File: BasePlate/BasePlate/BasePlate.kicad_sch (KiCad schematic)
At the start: 10 parts, among them J1 JST_BM04B-GHS-TBT, J2 1586842-6, J3 JST_BM03B-GHS-TBT, J4 JST_BM04B-GHS-TBT, J5 JST_BM04B-GHS-TBT, J6 JST_BM04B-GHS-TBT, J7 JST_BM04B-GHS-TBT, J8 JST_BM04B-GHS-TBT

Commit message: mostly finished
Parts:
- removed J8: JST_BM04B-GHS-TBT, bots:JST_BM04B-GHS-TBT, symbol thebots_symlib:JST_BM04B-GHS-TBT
- added H1, H2, H3, H4, H5, H6, H7, H8: MountingHole_Pad, TestPoint:TestPoint_Pad_D4.0mm, symbol Mechanical:MountingHole_Pad
- added J8: Conn_01x03_Socket, Connector_PinSocket_2.54mm:PinSocket_1x03_P2.54mm_Vertical, symbol Connector:Conn_01x03_Socket
- added J9: Conn_01x02_Socket, Connector_PinSocket_2.54mm:PinSocket_1x02_P2.54mm_Vertical, symbol Connector:Conn_01x02_Socket
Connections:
- net CAN+ is gone; now on net CAN_P: J1.2, JP1.1 (A)
- net CAN- is gone; now on net CAN_N: J1.3, R1.2
- net +5V: now also J8.2 (Pin_2), J9.1 (Pin_1)
- net BKBM: now also J8.1 (Pin_1)
- net GND: now also H1.1, H3.1, H5.1, H7.1, J8.3 (Pin_3), J9.2 (Pin_2)
- net VCC: now also H2.1, H4.1, H6.1, H8.1
- net CAN_P: now reaches J6.2
- net CAN_P: now also J4.2, J5.2, J7.2
- net CAN_N: now reaches J6.3
- net CAN_N: now also J4.3, J5.3, J7.3
- no-connect marks 14 -> 11

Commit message: baseplate
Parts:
- removed H1, H2, H3, H4, H5, H6, H7, H8: MountingHole_Pad, TestPoint:TestPoint_Pad_D4.0mm, symbol Mechanical:MountingHole_Pad
- removed JP1: Jumper_2_Bridged, Connector_PinHeader_2.54mm:PinHeader_1x02_P2.54mm_Vertical, symbol thebots_symlib:Jumper_2_Bridged
- added H1, H2, H3, H4, H5, H6, H7, H8: SMD_Pad_VBAT, thebots_baseplate:TestPoint_Pad_D4.0mm, symbol thebots_symlib:SMD_Pad_VBAT
- added JP1: Jumper_2_Bridged_smd, thebots_baseplate:PinHeader_1x02_P2.54mm_Vertical_SMD_Pin1Left, symbol thebots_symlib:Jumper_2_Bridged_smd
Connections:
- net CAN_P: now also JP1.1 (A)
- net GND: now also H1.1, H3.1, H5.1, H7.1
- net VCC: now also H2.1, H4.1, H6.1, H8.1
- net at R1.1: now also JP1.2 (B)

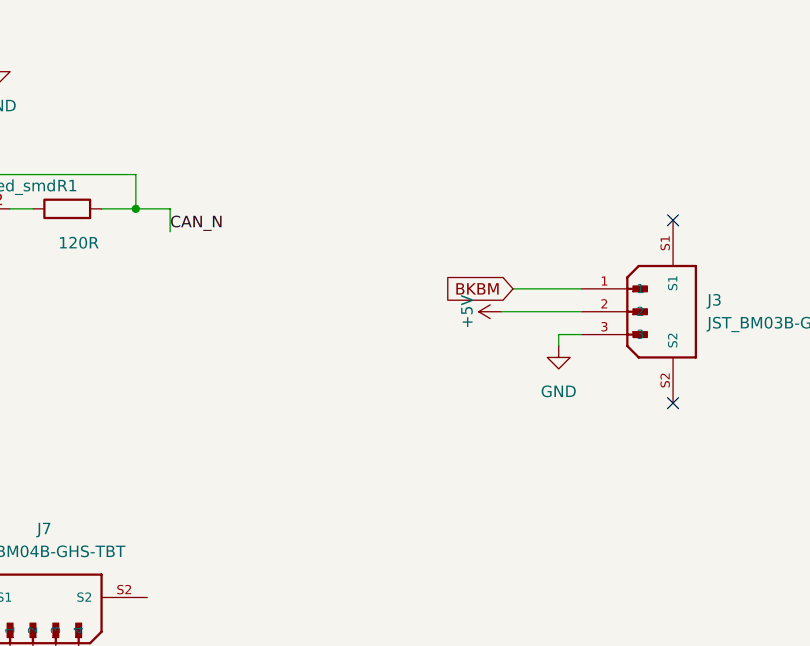
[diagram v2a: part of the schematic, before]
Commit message: wip breakbeam voltage divider
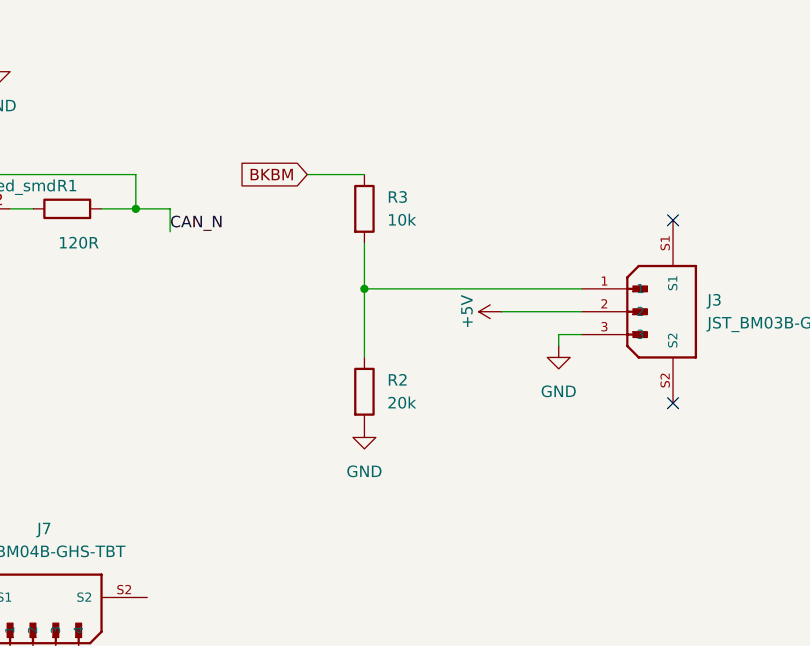
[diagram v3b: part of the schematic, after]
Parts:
- added R2: 20k, Resistor_SMD:R_0603_1608Metric, symbol Device:R
- added R3: 10k, Resistor_SMD:R_0603_1608Metric, symbol Device:R
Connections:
- net BKBM: now also R3.1; no longer J3.1
- net GND: now also R2.2
- new net: J3.1, R2.1, R3.2
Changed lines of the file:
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@@
+	)
+	(junction
+		(at 162.56 124.46)
+		(diameter 0)
+		(color 0 0 0 0)
 	)
 	(junction
@@
 	(wire
 		(pts
+			(xy 156.21 111.76) (xy 162.56 111.76)
+		)
+		(stroke
+			(width 0)
+			(type default)
+		)
+	)
+	(wire
+		(pts
 			(xy 123.19 115.57) (xy 125.73 115.57)
 		)
@@
 	(wire
 		(pts
+			(xy 162.56 119.38) (xy 162.56 124.46)
+		)
+		(stroke
+			(width 0)
+			(type default)
+		)
+	)
+	(wire
+		(pts
 			(xy 184.15 86.36) (xy 184.15 91.44)
 		)
@@
 	(wire
 		(pts
+			(xy 162.56 124.46) (xy 186.69 124.46)
+		)
+		(stroke
+			(width 0)
+			(type default)
+		)
+	)
+	(wire
+		(pts
 			(xy 171.45 78.74) (xy 171.45 83.82)
 		)
@@
 	(wire
 		(pts
-			(xy 179.07 124.46) (xy 186.69 124.46)
-		)
-		(stroke
-			(width 0)
-			(type default)
-		)
-	)
-	(wire
-		(pts
 			(xy 109.22 90.17) (xy 111.76 90.17)
 		)
@@
 		(pts
 			(xy 140.97 115.57) (xy 137.16 115.57)
+		)
+		(stroke
+			(width 0)
+			(type default)
+		)
+	)
+	(wire
+		(pts
+			(xy 162.56 124.46) (xy 162.56 132.08)
 		)
 		(stroke
@@
 	(global_label "BKBM"
 		(shape input)
-		(at 179.07 124.46 180)
+		(at 156.21 111.76 180)
 		(fields_autoplaced yes)
 		(effects
@@
 		)
 		(property "Intersheetrefs" "${INTERSHEET_REFS}"
-			(at 170.8234 124.46 0)
+			(at 147.9634 111.76 0)
 			(effects
 				(font
@@
 				(path "/bbc21205-8f0b-4bb2-8208-e4469bfb9468"
 					(reference "J2")
+					(unit 1)
+				)
+			)
+		)
+	)
+	(symbol
+		(lib_id "power:GND")
+		(at 162.56 139.7 0)
+		(unit 1)
+		(exclude_from_sim no)
+		(in_bom yes)
+		(on_board yes)
+		(dnp no)
+		(fields_autoplaced yes)
+		(property "Reference" "#PWR019"
+			(at 162.56 146.05 0)
+			(effects
+				(font
+					(size 1.27 1.27)
+				)
+				(hide yes)
+			)
+		)
+		(property "Value" "GND"
+			(at 162.56 144.78 0)
+			(effects
+				(font
+					(size 1.27 1.27)
+				)
+			)
+		)
+		(property "Footprint" ""
+			(at 162.56 139.7 0)
+			(effects
+				(font
+					(size 1.27 1.27)
+				)
+				(hide yes)
+			)
+		)
+		(property "Datasheet" ""
+			(at 162.56 139.7 0)
+			(effects
+				(font
+					(size 1.27 1.27)
+				)
+				(hide yes)
+			)
+		)
+		(property "Description" ""
+			(at 162.56 139.7 0)
+			(effects
+				(font
+					(size 1.27 1.27)
+				)
+				(hide yes)
+			)
+		)
+		(pin "1"
+		)
+		(instances
+			(project "BasePlate"
+				(path "/bbc21205-8f0b-4bb2-8208-e4469bfb9468"
+					(reference "#PWR019")
+					(unit 1)
+				)
+			)
+		)
+	)
+	(symbol
+		(lib_id "Device:R")
+		(at 162.56 115.57 0)
+		(unit 1)
+		(exclude_from_sim no)
+		(in_bom yes)
+		(on_board yes)
+		(dnp no)
+		(fields_autoplaced yes)
+		(property "Reference" "R3"
+			(at 165.1 114.2999 0)
+			(effects
+				(font
+					(size 1.27 1.27)
+				)
+				(justify left)
+			)
+		)
+		(property "Value" "10k"
+			(at 165.1 116.8399 0)
+			(effects
+				(font
+					(size 1.27 1.27)
+				)
+				(justify left)
+			)
+		)
+		(property "Footprint" "Resistor_SMD:R_0603_1608Metric"
+			(at 160.782 115.57 90)
+			(effects
+				(font
+					(size 1.27 1.27)
+				)
+				(hide yes)
+			)
+		)
+		(property "Datasheet" "~"
+			(at 162.56 115.57 0)
+			(effects
+				(font
+					(size 1.27 1.27)
+				)
+				(hide yes)
+			)
+		)
+		(property "Description" "Resistor"
+			(at 162.56 115.57 0)
+			(effects
+				(font
+					(size 1.27 1.27)
+				)
+				(hide yes)
+			)
+		)
+		(pin "1"
+		)
+		(pin "2"
+		)
+		(instances
+			(project "BasePlate"
+				(path "/bbc21205-8f0b-4bb2-8208-e4469bfb9468"
+					(reference "R3")
 					(unit 1)
 				)
@@
 					(unit 1)
 				)
+			)
+		)
+	)
+	(symbol
+		(lib_id "Device:R")
+		(at 162.56 135.89 0)
+		(unit 1)
+		(exclude_from_sim no)
+		(in_bom yes)
+		(on_board yes)
+		(dnp no)
+		(fields_autoplaced yes)
+		(property "Reference" "R2"
+			(at 165.1 134.6199 0)
+			(effects
+				(font
+					(size 1.27 1.27)
+				)
+				(justify left)
+			)
+		)
+		(property "Value" "20k"
+			(at 165.1 137.1599 0)
+			(effects
+				(font
+					(size 1.27 1.27)
+				)
+				(justify left)
+			)
+		)
+		(property "Footprint" "Resistor_SMD:R_0603_1608Metric"
+			(at 160.782 135.89 90)
+			(effects
+				(font
+					(size 1.27 1.27)
+				)
+				(hide yes)
+			)
+		)
+		(property "Datasheet" "~"
+			(at 162.56 135.89 0)
+			(effects
+				(font
+					(size 1.27 1.27)
+				)
+				(hide yes)
+			)
+		)
+		(property "Description" "Resistor"
+			(at 162.56 135.89 0)
+			(effects
+				(font
+					(size 1.27 1.27)
+				)
+				(hide yes)
+			)
+		)
+		(pin "1"
+		)
+		(pin "2"
+		)
+		(instances
+			(project "BasePlate"
+				(path "/bbc21205-8f0b-4bb2-8208-e4469bfb9468"
+					(reference "R2")
+					(unit 1)
+				)

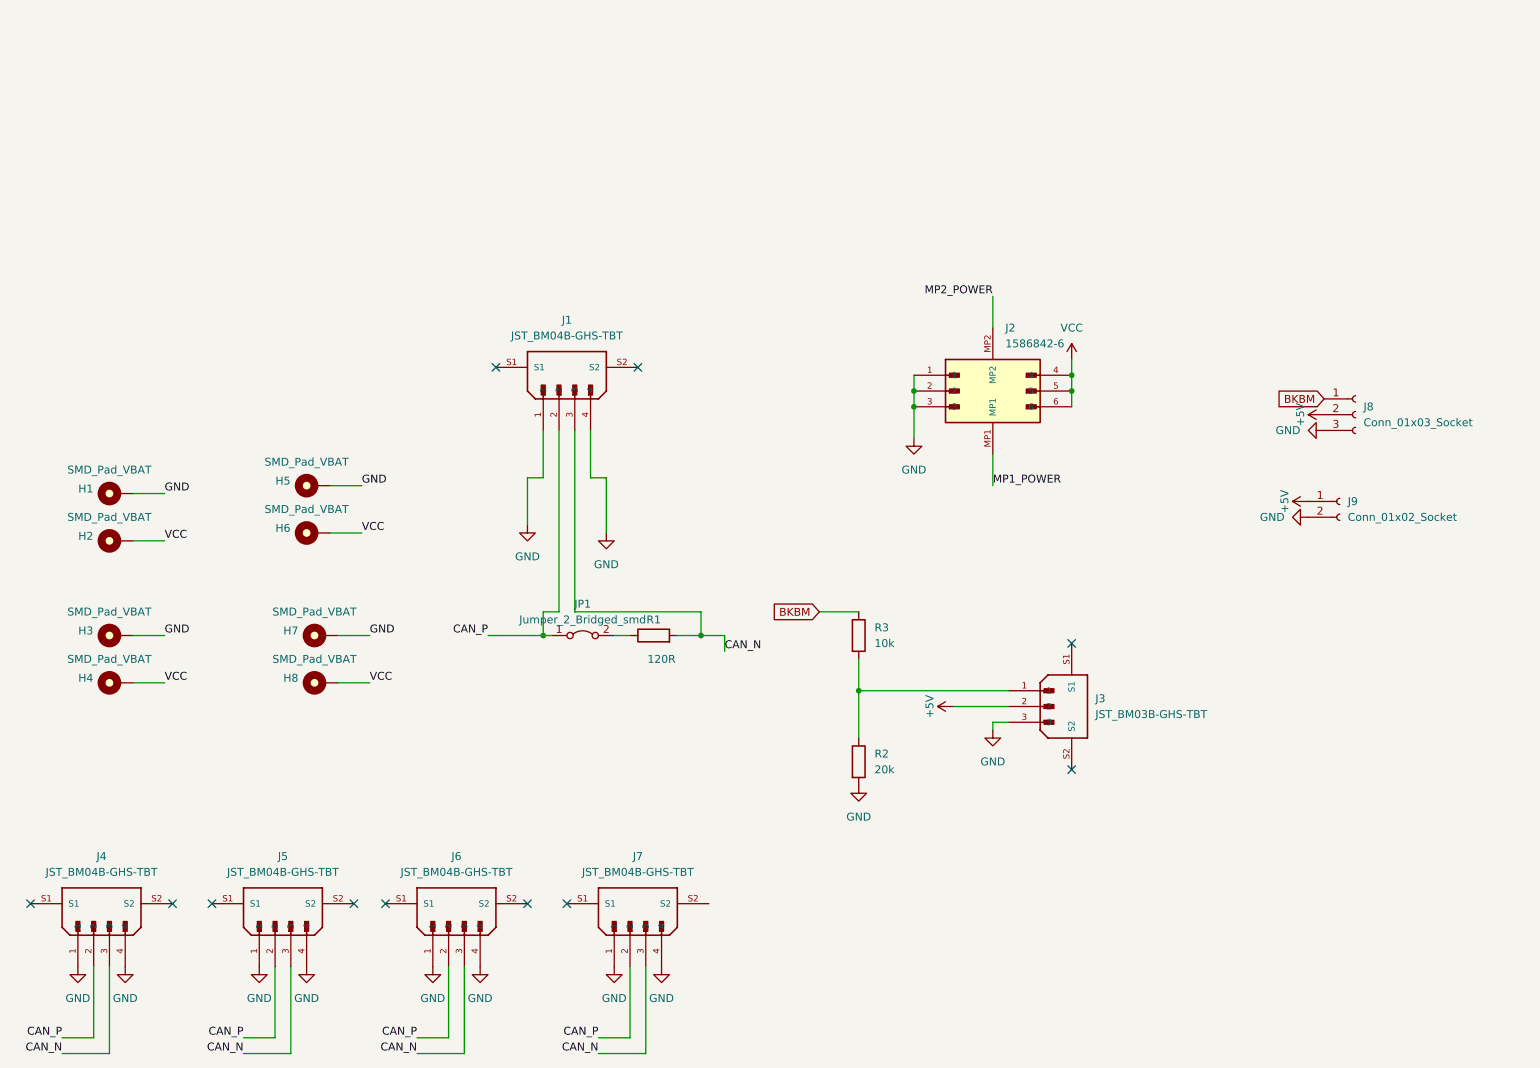
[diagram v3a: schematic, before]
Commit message: skidplate, then realized its pointless
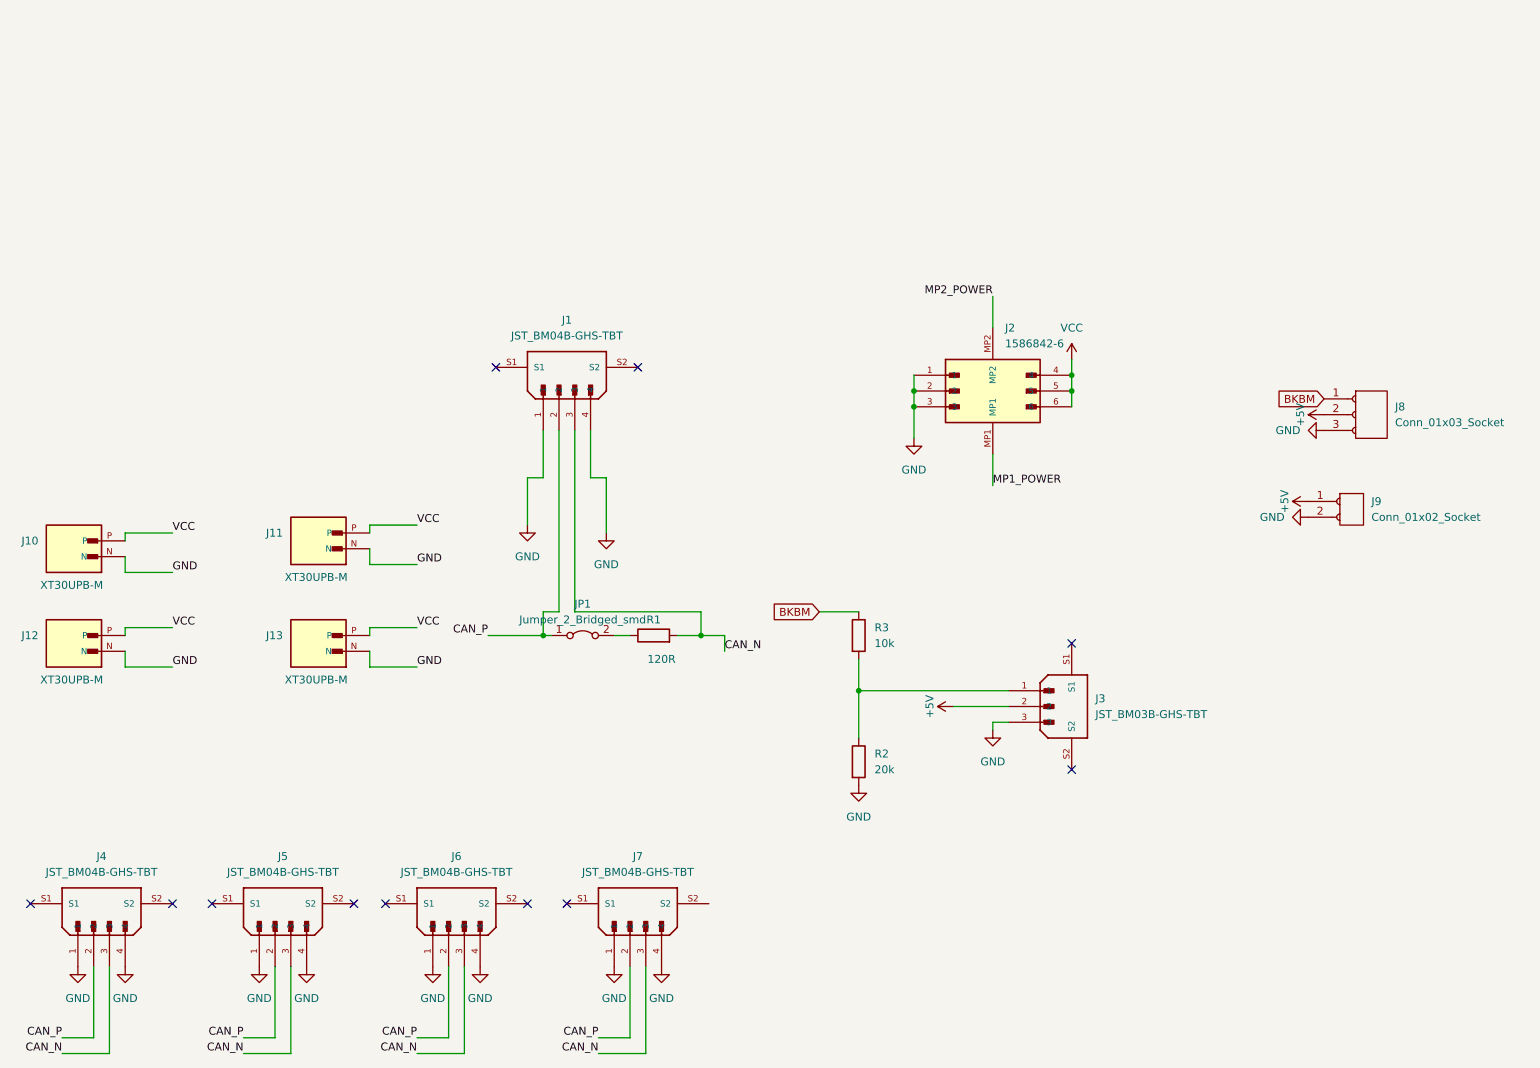
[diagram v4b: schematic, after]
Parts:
- removed H1, H2, H3, H4, H5, H6, H7, H8: SMD_Pad_VBAT, thebots_baseplate:TestPoint_Pad_D4.0mm, symbol thebots_symlib:SMD_Pad_VBAT
- added J10, J11, J12, J13: XT30UPB-M, bots:AMASS_XT30UPB-M, symbol bots:XT30UPB-M
- J1, J4, J5, J6, J7: symbol thebots_symlib:JST_BM04B-GHS-TBT -> bots:JST_BM04B-GHS-TBT
- J2: symbol thebots_symlib:TE_1586842-6_6PIN -> bots:TE_1586842-6_6PIN
- J3: symbol thebots_symlib:JST_BM03B-GHS-TBT -> bots:JST_BM03B-GHS-TBT
- J8: footprint Connector_PinSocket_2.54mm:PinSocket_1x03_P2.54mm_Vertical -> bots:PinSocket_1x03_P2.54mm_Vertical; symbol Connector:Conn_01x03_Socket -> bots:Conn_01x03_Socket
- J9: footprint Connector_PinSocket_2.54mm:PinSocket_1x02_P2.54mm_Vertical -> bots:PinSocket_1x02_P2.54mm_Vertical; symbol Connector:Conn_01x02_Socket -> bots:Conn_01x02_Socket
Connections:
- net GND: now also J10.N, J11.N, J12.N, J13.N
- net VCC: now also J10.P, J11.P, J12.P, J13.P

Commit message: baseplate
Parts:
- removed JP1: Jumper_2_Bridged_smd, thebots_baseplate:PinHeader_1x02_P2.54mm_Vertical_SMD_Pin1Left, symbol thebots_symlib:Jumper_2_Bridged_smd
- added JP1: Jumper_2_Bridged_smd, bots:PinHeader_1x02_P2.54mm_Vertical_SMD_Pin1Left, symbol bots:Jumper_2_Bridged_smd
- added R4: 0R, bots:R_0603_1608Metric, symbol bots:R_0R
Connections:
- net CAN_P: now also R4.1
- net jumper_N: now reaches R1.1
- net jumper_N: now also JP1.1 (A)
- new net jumper_P: JP1.2 (B), R4.2
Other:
- note added: "Matching resistor for length"
- moved on the sheet: J1, R1

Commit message: baseplate v1.1
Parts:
- removed J8: Conn_01x03_Socket, bots:PinSocket_1x03_P2.54mm_Vertical, symbol bots:Conn_01x03_Socket
- removed J9: Conn_01x02_Socket, bots:PinSocket_1x02_P2.54mm_Vertical, symbol bots:Conn_01x02_Socket
- removed JP1: Jumper_2_Bridged_smd, bots:PinHeader_1x02_P2.54mm_Vertical_SMD_Pin1Left, symbol bots:Jumper_2_Bridged_smd
- removed R4: 0R, bots:R_0603_1608Metric, symbol bots:R_0R
- added J14: XT30UPB-M, bots:AMASS_XT30UPB-M, symbol bots:XT30UPB-M
- added J15: JST_B3B-XH-A, bots:JST_B3B-XH-A, symbol bots:JST_B3B-XH-A
- added J8: JST_BM04B-GHS-TBT, bots:JST_BM04B-GHS-TBT, symbol bots:JST_BM04B-GHS-TBT
- added J9: XH 2 Pin, bots:JST_B2B-XH-A_LF__SN_, symbol bots:JST_B2B-XH-A
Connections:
- net jumper_N is gone; now on net CAN_N: R1.1
- net +5V: now also J15.2, J9.1
- net BKBM: now also J15.1
- net CAN_N: now also J8.3; no longer R1.2
- net CAN_P: now also R1.2, J8.2
- net GND: now also J14.N, J15.3, J8.1, J8.4, J9.2
- net VCC: now also J14.P
- no-connect marks 11 -> 13
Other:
- note added: "Dribbler"
- moved on the sheet: R1

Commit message: update
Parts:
- added H1, H2, H3, H4: 24929, bots:Keystone_24929, symbol bots:ZeroH_Keystone24929_Pad
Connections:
- net +5V: now also J15.3, J9.2; no longer J15.2, J9.1
- net BKBM: now also J15.2; no longer J15.1
- net GND: now also J15.1, J9.1; no longer J15.3, J9.2
- no-connect marks 13 -> 14
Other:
- note added: "Breakbeam Input"
- note added: "CAN Connectors (motor drives)"
- note added: "CAN Input"
- note added: "Power Connectors (motor drives)"
- note added: "Power Input"
- note added: "Zero Height Standoffs (for threading into the board)"
- note removed: "Matching resistor for length"
- moved on the sheet: J1, J15, J2, J3, J4, J5, J6, J7, J8, J9, R1, R2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

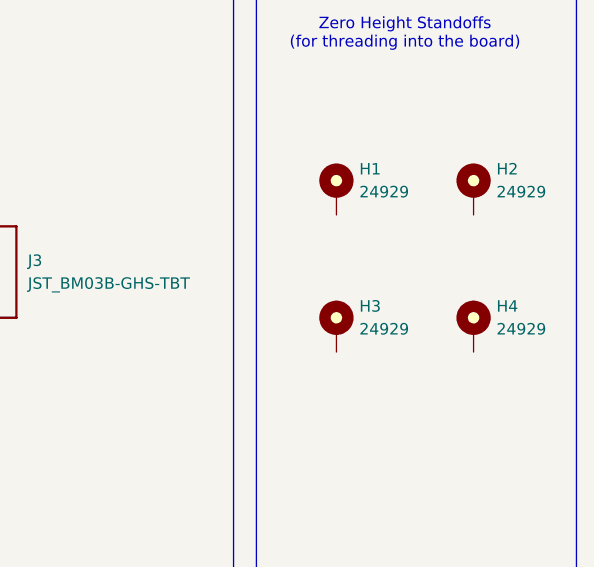
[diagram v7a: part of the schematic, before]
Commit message: baseplate zeroH standoffs
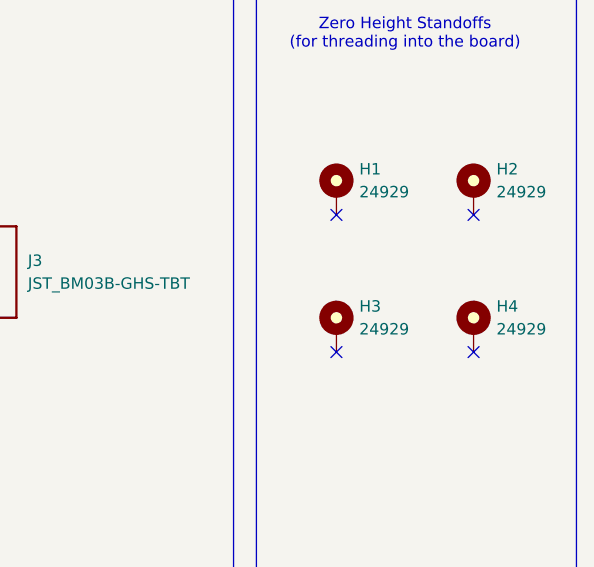
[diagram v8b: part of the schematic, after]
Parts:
- H1, H2, H3, H4: JLC (none) -> SMD; LCSC (none) -> C20631974
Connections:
- no-connect marks 14 -> 18
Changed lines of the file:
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@@
 	)
 	(no_connect
+		(at 256.54 54.61)
+	)
+	(no_connect
 		(at 203.2 55.88)
 	)
@@
 	)
 	(no_connect
+		(at 256.54 39.37)
+	)
+	(no_connect
 		(at 185.42 135.89)
 	)
@@
 	)
 	(no_connect
+		(at 241.3 54.61)
+	)
+	(no_connect
+		(at 241.3 39.37)
+	)
+	(no_connect
 		(at 81.28 135.89)
 	)
@@
 			)
 		)
+		(property "LCSC" "C20631974"
+			(at 256.54 52.07 0)
+			(hide yes)
+			(show_name no)
+			(do_not_autoplace no)
+			(effects
+				(font
+					(size 1.27 1.27)
+				)
+			)
+		)
+		(property "JLC" "SMD"
+			(at 256.54 52.07 0)
+			(hide yes)
+			(show_name no)
+			(do_not_autoplace no)
+			(effects
+				(font
+					(size 1.27 1.27)
+				)
+			)
+		)
 		(pin "1"
 		)
@@
 			)
 		)
+		(property "LCSC" "C20631974"
+			(at 241.3 36.83 0)
+			(hide yes)
+			(show_name no)
+			(do_not_autoplace no)
+			(effects
+				(font
+					(size 1.27 1.27)
+				)
+			)
+		)
+		(property "JLC" "SMD"
+			(at 241.3 36.83 0)
+			(hide yes)
+			(show_name no)
+			(do_not_autoplace no)
+			(effects
+				(font
+					(size 1.27 1.27)
+				)
+			)
+		)
 		(pin "1"
 		)
@@
 			)
 		)
+		(property "LCSC" "C20631974"
+			(at 256.54 36.83 0)
+			(hide yes)
+			(show_name no)
+			(do_not_autoplace no)
+			(effects
+				(font
+					(size 1.27 1.27)
+				)
+			)
+		)
+		(property "JLC" "SMD"
+			(at 256.54 36.83 0)
+			(hide yes)
+			(show_name no)
+			(do_not_autoplace no)
+			(effects
+				(font
+					(size 1.27 1.27)
+				)
+			)
+		)
 		(pin "1"
 		)
@@
 			(at 241.3 52.07 0)
 			(hide yes)
+			(show_name no)
+			(do_not_autoplace no)
+			(effects
+				(font
+					(size 1.27 1.27)
+				)
+			)
+		)
+		(property "LCSC" "C20631974"
+			(at 241.3 52.07 0)
+			(hide yes)
+			(show_name no)
+			(do_not_autoplace no)
+			(effects
+				(font
+					(size 1.27 1.27)
+				)
+			)
+		)
+		(property "JLC" "SMD"
+			(at 241.3 52.07 0)
+			(hide yes)
